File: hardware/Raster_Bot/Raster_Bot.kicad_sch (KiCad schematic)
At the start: 65 parts, among them J1 JST_PH, J2 USB_C_Receptacle_USB2.0_16P, J3 Conn_EYESPI, J4 Conn_Motor_N20_Encoder, J6 Conn_Motor_N20_Encoder, Q1 AO3401A, Q2 AO3401A, Q3 2N7002, SW1 SW_SPDT_SH, SW2 SW_RESET, SW3 SW_BOOT, U1 AP2114H-3.3, U2 BQ24072RGT, U3 ESP32-S3-MINI-1, U4 TPS61023DRLR, U5 DRV8833PWPR

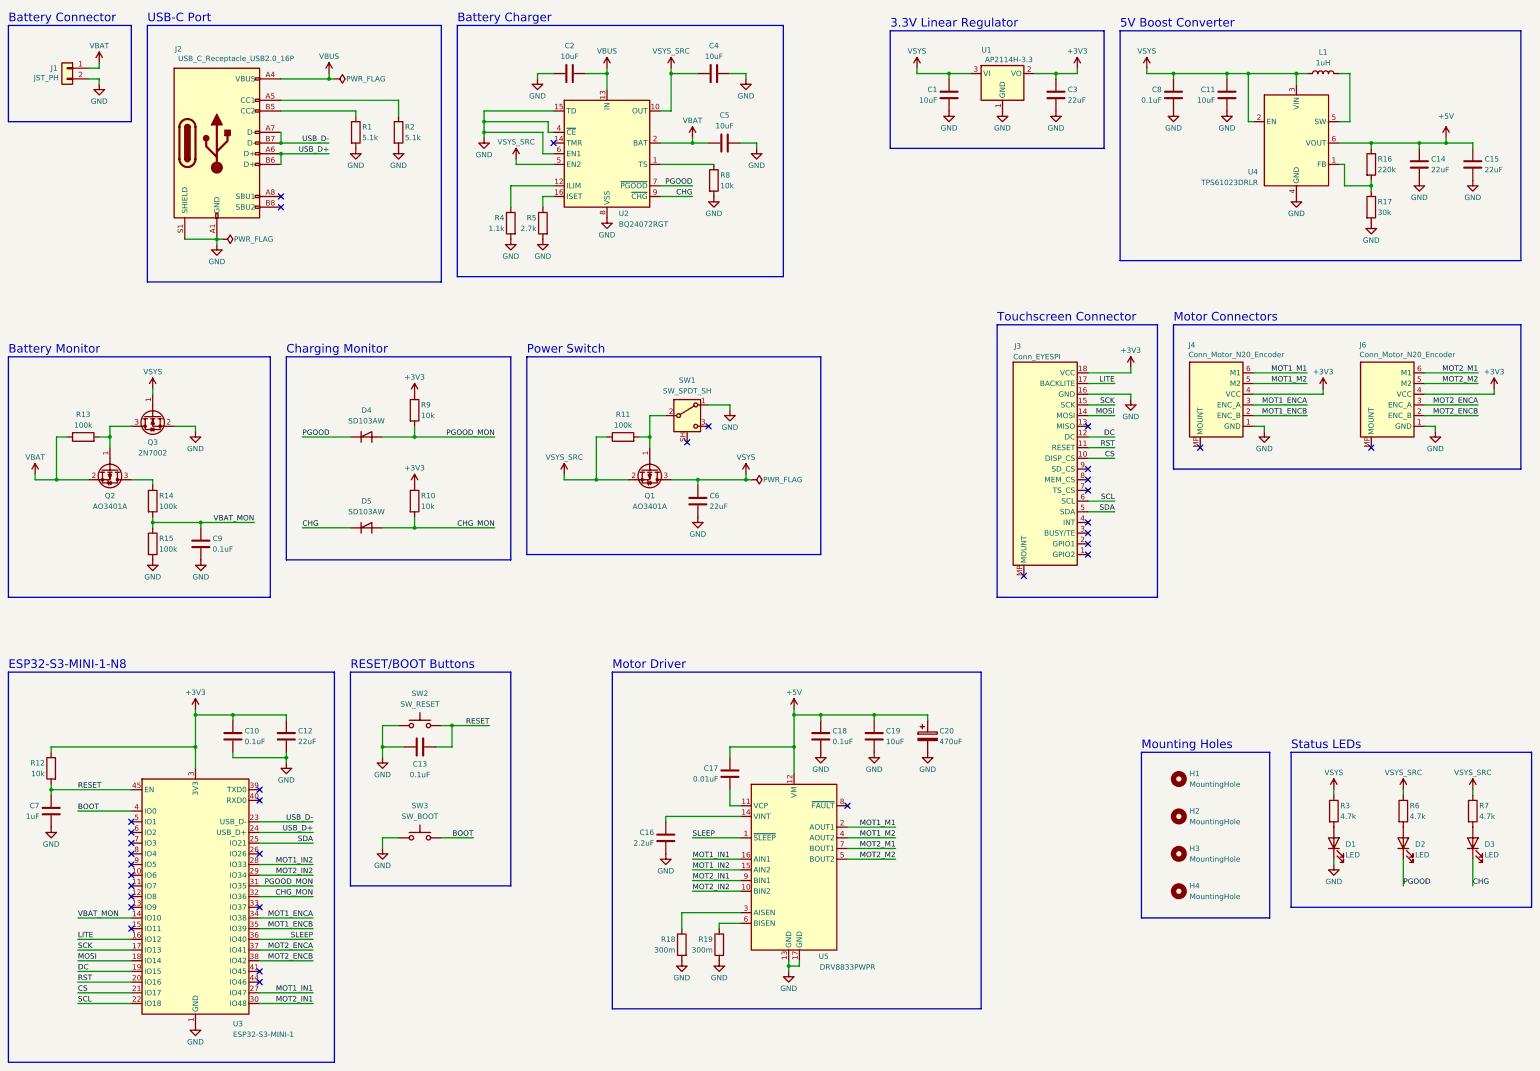
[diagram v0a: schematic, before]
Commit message: [hardware] v0.7 - Added bulk capacitance; PCB layout update
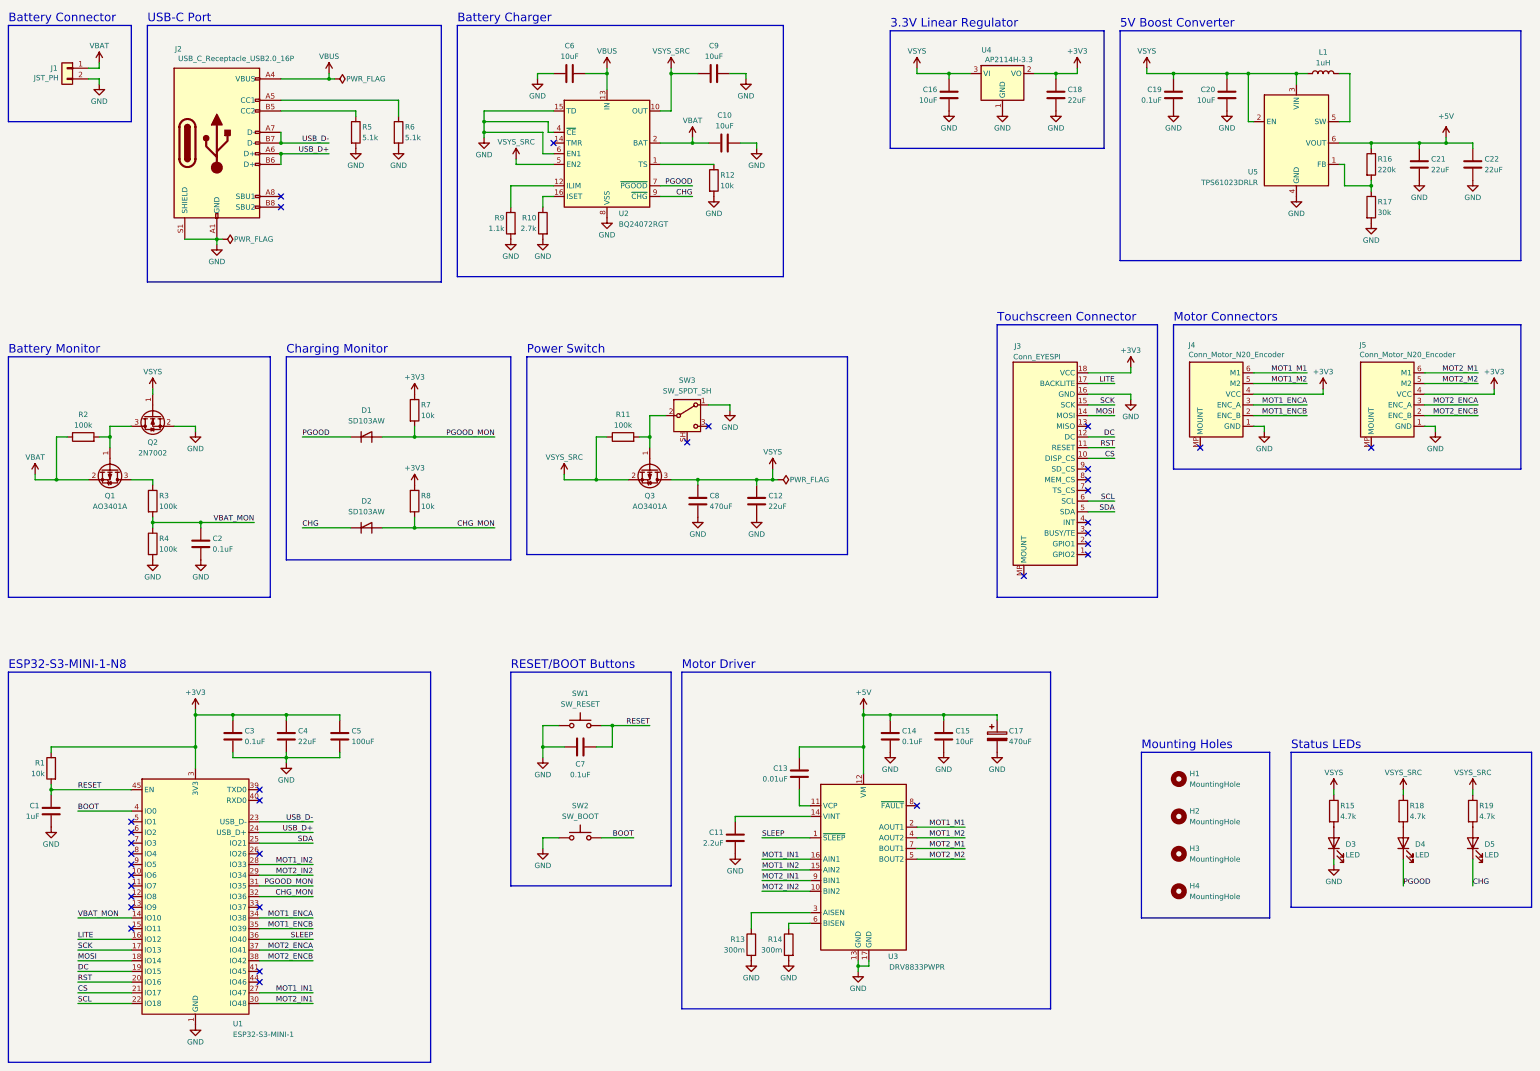
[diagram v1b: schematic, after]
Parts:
- added C5: 100uF, Capacitor_SMD:C_1206_3216Metric, symbol Device:C
- added C8: 470uF, Capacitor_SMD:CP_Elec_6.3x7.7, symbol Device:C
- renumbered C7 to C1, C5 to C10, C16 to C11, C6 to C12, C17 to C13, C18 to C14, C19 to C15, C1 to C16, C20 to C17, C3 to C18, C8 to C19, C9 to C2, C11 to C20, C14 to C21, C15 to C22, C10 to C3, C12 to C4, C2 to C6, C13 to C7, C4 to C9, D4 to D1, D5 to D2, D1 to D3, D2 to D4, D3 to D5, J6 to J5, Q2 to Q1, Q3 to Q2, Q1 to Q3, R12 to R1, R5 to R10, R8 to R12, R18 to R13, R19 to R14, R3 to R15, R6 to R18, R7 to R19, R13 to R2, R14 to R3, R15 to R4, R1 to R5, R2 to R6, R9 to R7, R10 to R8, R4 to R9, SW2 to SW1, SW3 to SW2, SW1 to SW3, U3 to U1, U5 to U3, U1 to U4, U4 to U5
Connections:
- net +3V3: now also C5.1
- net GND: now also C5.2, C8.2
- net VSYS: now also C8.1
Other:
- moved on the sheet: C11, C12, C13, C14, C15, C17, C7, R13, R14, SW1, SW2, U3
